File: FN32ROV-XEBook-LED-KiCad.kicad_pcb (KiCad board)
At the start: 2 copper layers, 40 x 10 mm, 6 parts, among them J1 LED_JST

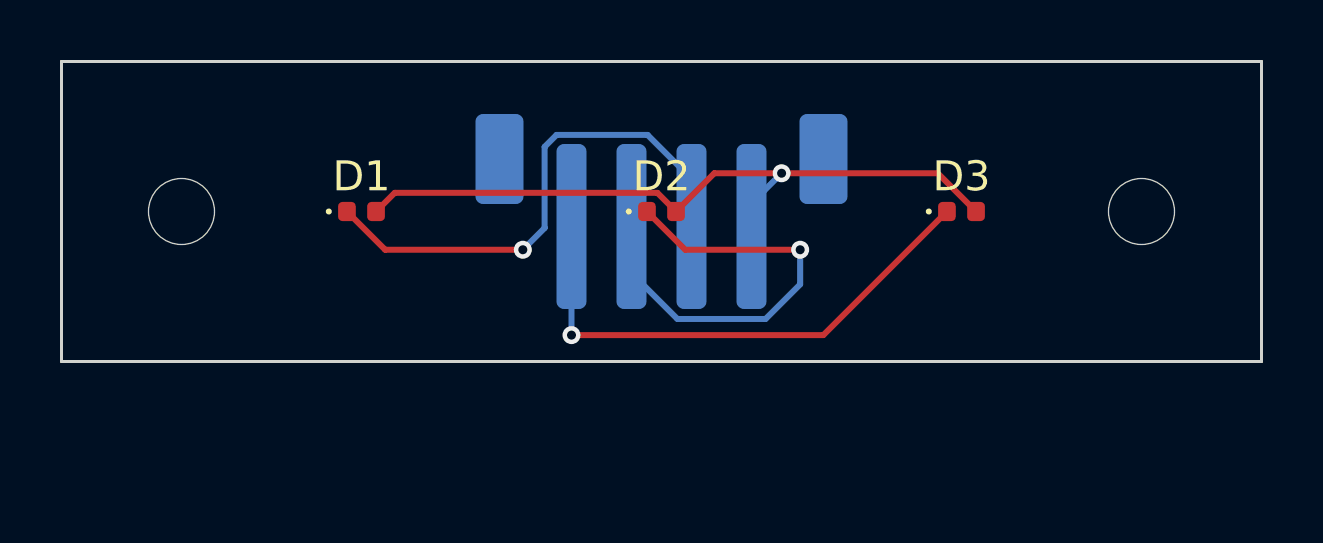
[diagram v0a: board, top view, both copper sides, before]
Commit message: Switch J1 back to through-hole, grow board to 40x14mm, add logo, export fab files
Assembling both sides (SMD LEDs on front + SMD JST on back) was too costly for
JLCPCB assembly, so J1 reverts to through-hole and gets hand-soldered instead.
That meant reworking the board height and LED/connector Y-offsets so the
through-hole housing does not physically collide with the case light-pipe
housings (the earlier SMD-based clearance math did not carry over, since THT
housings are much deeper than the SMD footprint was).

Board is now 40x14mm: LEDs at y=3mm, mounting holes + J1 housing edge on the
y=7mm row, J1 pad row at y=9.2mm. Logo centered exactly on the back silkscreen.
LCSC part numbers recorded on each part in the schematic (D1=C471422,
D2=C30584803, D3=C28310436, J1=C265289). Fab export regenerated to match:
Gerbers, drill files, BOM/CPL (including a JLCPCB-Assembly-specific set that
excludes J1, since it is hand-soldered, not SMT-placed).

Co-Authored-By: Claude Sonnet 5 <noreply@anthropic.com>
Claude-Session: https://claude.ai/code/session_011E5FphyrLWBpYvbXpCPZfr
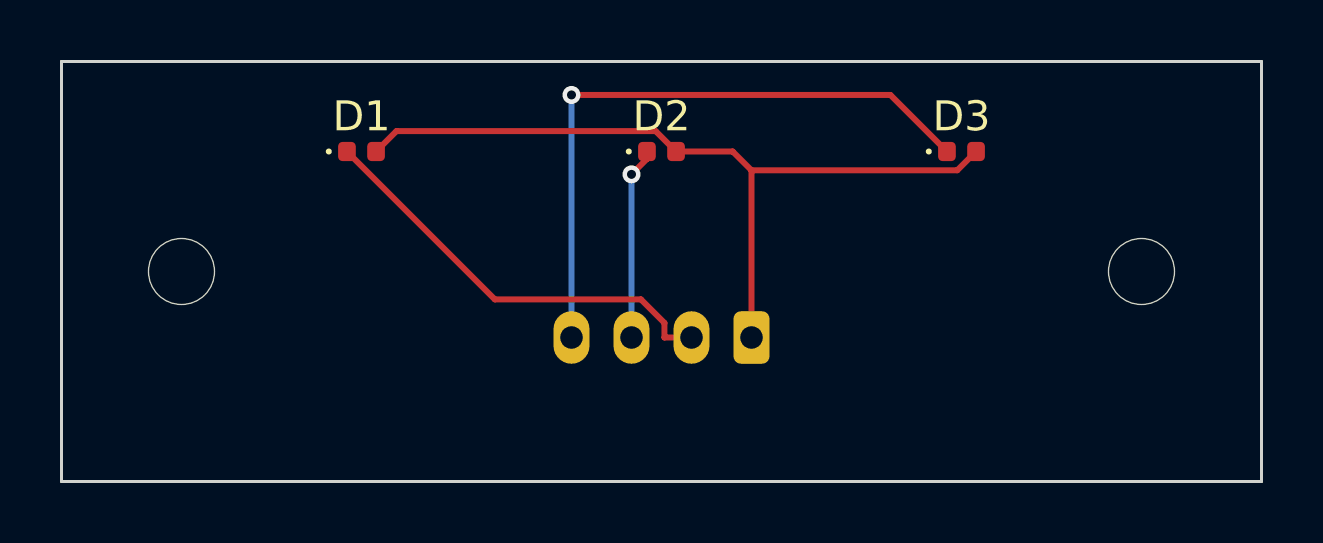
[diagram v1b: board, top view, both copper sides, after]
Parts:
- D1, D2, D3: footprint LED_0402_1005Metric -> LED_SMD:LED_0402_1005Metric
- J1: footprint JST_PH_B4B-PH-SM4-TB_1x04-1MP_P2.00mm_Vertical -> Connector_JST:JST_PH_B4B-PH-K_1x04_P2.00mm_Vertical
- moved J1 5.16 mm to (123.0, 109.2)
- moved D1 2.00 mm to (110.0, 103.0)
- moved D2 2.00 mm to (120.0, 103.0)
- moved D3 2.00 mm to (130.0, 103.0)
- moved MH1 2.00 mm to (104.0, 107.0)
- moved MH2 2.00 mm to (136.0, 107.0)
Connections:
- net 3V3 renamed /3V3
- net LED_BT renamed /LED_BT
- net LED_SIO renamed /LED_SIO
- net LED_WIFI renamed /LED_WIFI
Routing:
- net /LED_BT: track 15.1 -> 6.41 mm
- net /LED_SIO: track 17.8 -> 21.4 mm
- net /LED_WIFI: track 17.4 -> 14.3 mm, vias 1 -> 0
- net /3V3: track 23.8 -> 26.7 mm, vias 1 -> 0
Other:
- board size 40 x 10 mm -> 40 x 14 mm

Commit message: Silkscreen: add pin-1 marker to J1
Marks pin 1 on the cable header so the harness to the main board cannot
be seated backwards during assembly.

Verified against the previous commit: footprints, pads, copper segments,
vias and zone definitions are all unchanged. Only F.SilkS text was added
(plus zone refills and uuid churn from the save).

Co-Authored-By: Claude Opus 5 (1M context) <noreply@anthropic.com>
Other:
- board text added: "1"
